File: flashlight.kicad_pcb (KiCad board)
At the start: 2 copper layers, 45 x 120 mm, 23 parts, among them J1 USB_B_Micro, J2 Conn_01x03_Pin, Q2 HSS2333, SW1 SW_DIP_x01, U1 XB4908A, U2 MT3608, U3 TP4057, U4 R6BHC-A05_LED-19-223

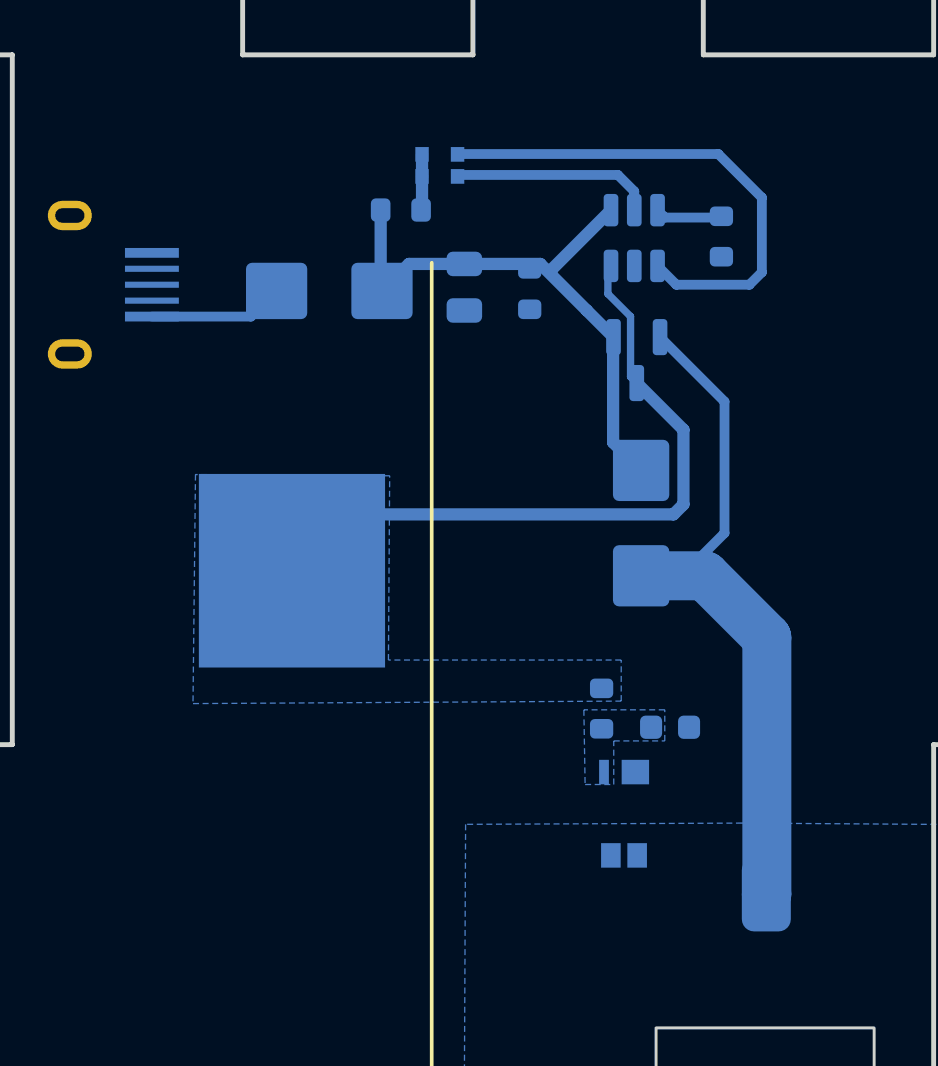
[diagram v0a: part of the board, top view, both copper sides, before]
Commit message: moved TP4057 closer to the VBAT
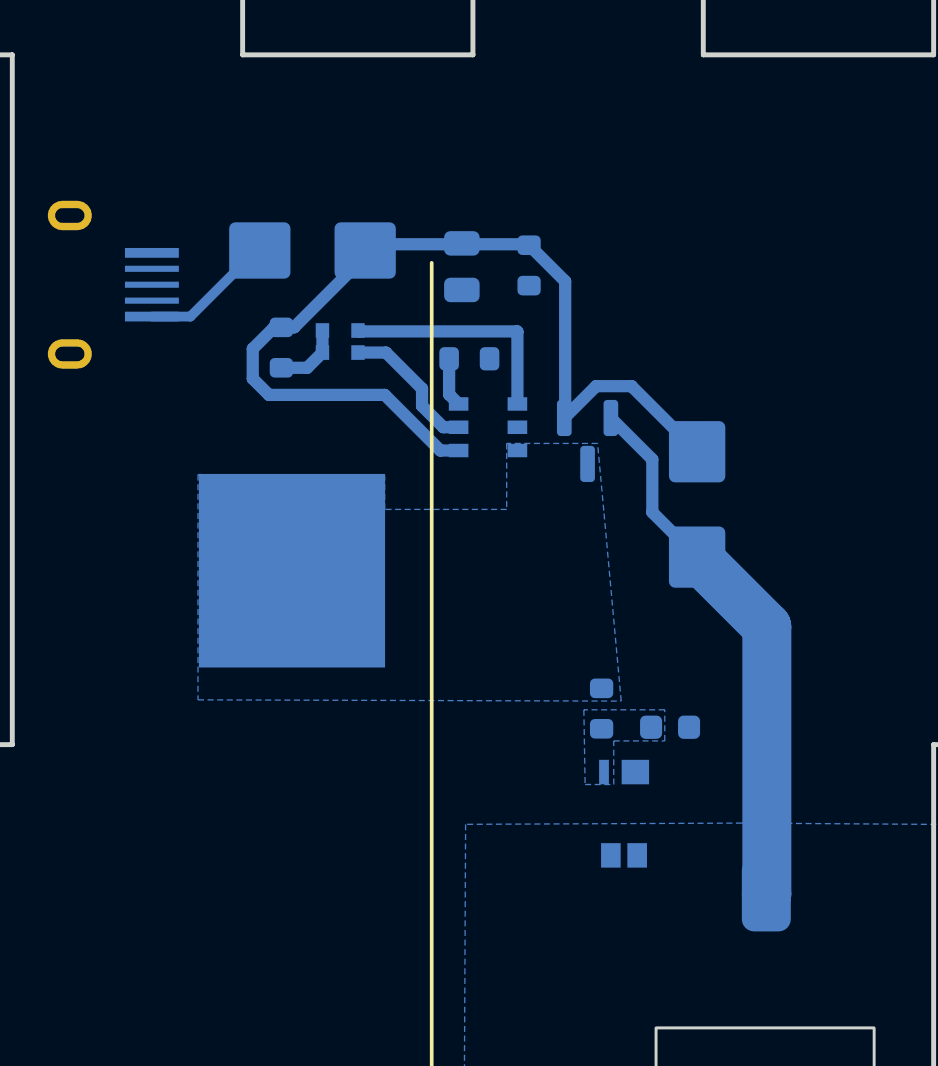
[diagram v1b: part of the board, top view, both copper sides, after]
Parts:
- U3: footprint Package_TO_SOT_SMD:TSOT-23-6 -> SparkFun-Semiconductor-Standard:SOT23-6-Tight
- moved R1 11.4 mm to (97.5, 51.9), turned to 0 degrees
- moved U3 9.76 mm to (98.3, 54.7), turned to 180 degrees
- moved U4 8.26 mm to (93.0, 50.7)
- moved R2 7.44 mm to (89.9, 51.5), turned to -90 degrees
- moved Q2 3.86 mm to (102.4, 55.3)
- moved D4 2.41 mm to (106.8, 57.9)
- moved D1 1.79 mm to (91.1, 47.5)
- moved R4 0.97 mm to (100.0, 48.1)
- moved C1 0.84 mm to (97.2, 48.2)
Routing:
- net Net-(BT1-+): track 28.0 -> 0.00 mm
- net Net-(D1-K): track 23.9 -> 38.8 mm
- net Net-(U3-~{CHRG}): track 21.0 -> 9.48 mm
- net Net-(D4-K): track 29.9 -> 22.1 mm
- net Net-(U3-STDBY): track 8.28 -> 5.78 mm
- net Net-(U3-PROG): track 2.58 -> 2.00 mm
- net Net-(U4-Blue+): track 2.29 -> 2.83 mm
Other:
- board text added: "V2.6"
- board text removed: "V2.5"

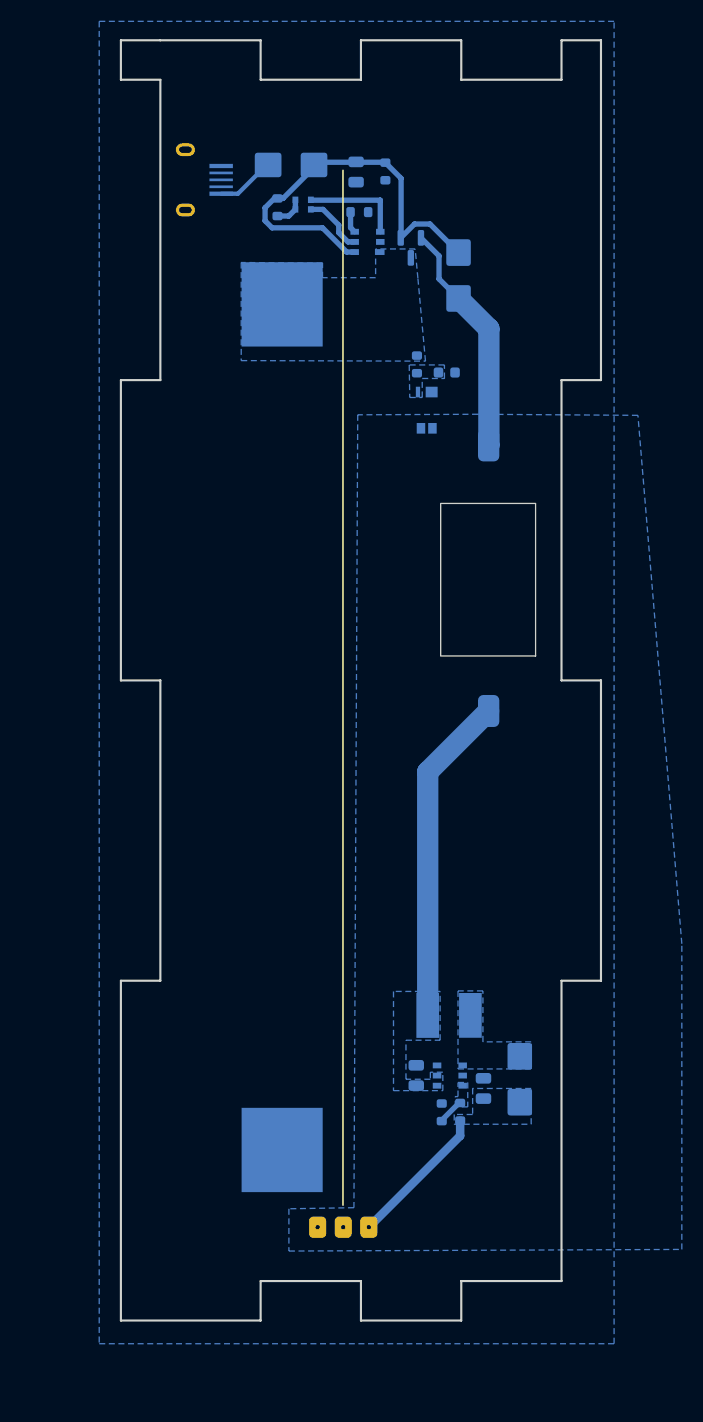
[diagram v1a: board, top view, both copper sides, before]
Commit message: v2.6: board outline 4mm
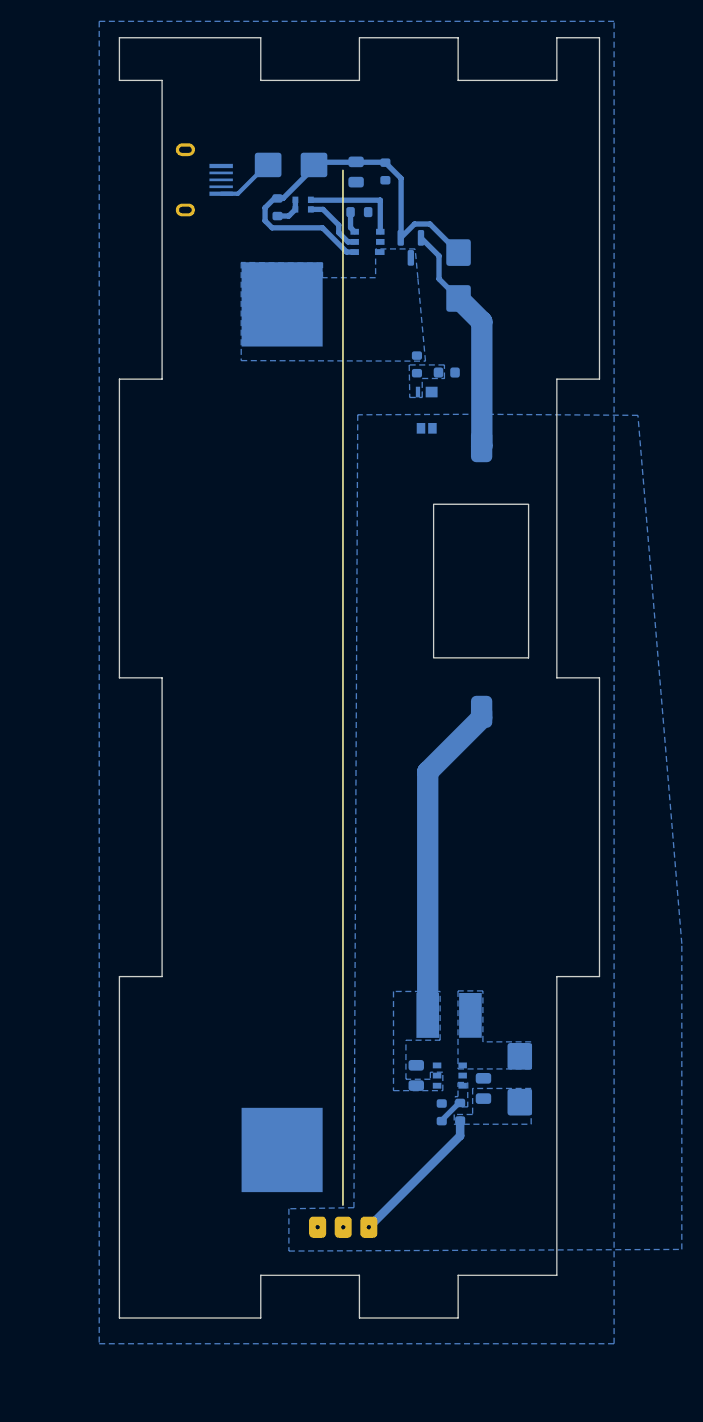
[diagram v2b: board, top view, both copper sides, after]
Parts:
- moved SW1 0.66 mm to (104.5, 79.5)
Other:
- outline, holes or cut-outs redrawn

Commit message: v2.7 boxes
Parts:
- removed SW1: SW_DIP_x01, FlashlightLib:KCD11-2P
- added U5: SS12J01_071, JLCPCB-SS12J01:SW-TH_SHOU-HAN_SS12J01, F.Cu at (109.2, 84.6)
- moved J1 1.30 mm to (82.5, 47.7)
- moved C3 1.20 mm to (102.9, 131.6)
- moved C4 1.20 mm to (109.2, 132.9)
- moved R6 1.20 mm to (105.3, 135.1)
- moved U2 1.20 mm to (106.0, 131.7)
- moved BT1 1.20 mm to (90.3, 99.0)
- moved C1 1.20 mm to (97.2, 47.0)
- moved C2 1.20 mm to (105.7, 65.8)
- moved Q2 1.20 mm to (102.4, 54.1)
- moved R1 1.20 mm to (97.5, 50.7)
- moved R2 1.20 mm to (89.9, 50.3)
- moved R3 1.20 mm to (102.9, 65.0)
- moved U1 1.20 mm to (103.1, 67.6)
- moved U4 1.20 mm to (93.0, 49.5)
- moved D1 1.20 mm to (91.1, 46.3)
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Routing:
- net Net-(U2-EN): track 30.5 -> 49.1 mm
- net Net-(D4-K): track 21.9 -> 36.2 mm
- net VOUT: track 13.5 -> 16.0 mm
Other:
- board size 45 x 120 mm -> 45.2 x 120.2 mm
- board text added: "DO NOT PRINT ON F LAYER!"
- board text added: "V2.7"
- board text added: "ВИМК"
- board text added: "УВІМК"
- board text removed: "V2.6"

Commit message: V3.0 21700 3x8 leds
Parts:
- removed J1: USB_B_Micro, FlashlightLib:USB-1101IPX6-02
- removed J2: Conn_01x03_Pin, FlashlightLib:LED_Strip
- added C4: 22uF/35V, Capacitor_SMD:C_0805_2012Metric, B.Cu at (109.0, 93.3)
- added C5: 10uF/10V, Capacitor_SMD:C_0603_1608Metric, B.Cu at (97.6, 51.8)
- added C6: 10uF/10V, Capacitor_SMD:C_0603_1608Metric, B.Cu at (93.4, 55.1)
- added D10: LED, footprint:LED-SMD_L3.0-W1.4-RD_WHITE, F.Cu at (81.8, 98.9)
- added D11: LED_Pad, footprint:LED-SMD_3P-L5.7-W3.0-RD, F.Cu at (84.4, 94.3)
- added D12: LED_Pad, footprint:LED-SMD_3P-L5.7-W3.0-RD, F.Cu at (95.7, 122.8)
- added D13: LED_Pad, footprint:LED-SMD_3P-L5.7-W3.0-RD, F.Cu at (95.7, 114.9)
- added D14: LED, footprint:LED-SMD_L3.0-W1.4-RD_WHITE, F.Cu at (91.2, 111.1)
- added D15: LED, footprint:LED-SMD_L3.0-W1.4-RD_WHITE, F.Cu at (95.5, 109.4)
- added D16: LED, footprint:LED-SMD_L3.0-W1.4-RD_WHITE, F.Cu at (100.1, 110.9)
- added D17: LED_Pad, footprint:LED-SMD_3P-L5.7-W3.0-RD, F.Cu at (95.7, 104.4)
- added D18: LED, footprint:LED-SMD_L3.0-W1.4-RD_WHITE, F.Cu at (95.9, 99.8)
- added D19: LED, footprint:LED-SMD_L3.0-W1.4-RD_WHITE, F.Cu at (95.6, 97.4)
- added D2: D_Schottky, Diode_SMD:D_SMB, B.Cu at (101.6, 53.9)
- added D20: LED_Pad, footprint:LED-SMD_3P-L5.7-W3.0-RD, F.Cu at (106.4, 94.7)
- added D21: LED, footprint:LED-SMD_L3.0-W1.4-RD_WHITE, F.Cu at (109.3, 99.2)
- added D22: LED_Pad, footprint:LED-SMD_3P-L5.7-W3.0-RD, F.Cu at (106.3, 102.3)
- added D23: LED_Pad, footprint:LED-SMD_3P-L5.7-W3.0-RD, F.Cu at (109.0, 109.3)
- added D24: LED, footprint:LED-SMD_L3.0-W1.4-RD_WHITE, F.Cu at (105.1, 110.8)
- added D25: LED_Pad, footprint:LED-SMD_3P-L5.7-W3.0-RD, F.Cu at (107.5, 114.9)
- added D26: LED, footprint:LED-SMD_L3.0-W1.4-RD_WHITE, F.Cu at (101.0, 114.6)
- added D27: LED_Pad, footprint:LED-SMD_3P-L5.7-W3.0-RD, F.Cu at (100.9, 119.7)
- added D28: LED_Pad, footprint:LED-SMD_3P-L5.7-W3.0-RD, F.Cu at (90.5, 119.7)
- added D3: LED, footprint:LED-SMD_L3.0-W1.4-RD_WHITE, F.Cu at (90.3, 114.6)
- added D6: LED_Pad, footprint:LED-SMD_3P-L5.7-W3.0-RD, F.Cu at (84.0, 115.0)
- added D7: LED, footprint:LED-SMD_L3.0-W1.4-RD_WHITE, F.Cu at (86.5, 111.0)
- added D8: LED_Pad, footprint:LED-SMD_3P-L5.7-W3.0-RD, F.Cu at (82.3, 109.2)
- added D9: LED_Pad, footprint:LED-SMD_3P-L5.7-W3.0-RD, F.Cu at (84.7, 101.8)
- added F2: BSMD1210-150-6V, Fuse:Fuse_1210_3225Metric, B.Cu at (84.9, 44.8)
- added FB1: FerriteBead, Inductor_SMD:L_0805_2012Metric, B.Cu at (87.1, 47.5)
- added G***: LOGO, LOGO, F.Cu at (76.7, 69.3)
- added G***: LOGO, LOGO, F.Cu at (99.0, 74.0)
- added H1: MountingHole, FlashlightLib:M4-insert, F.Cu at (77.7, 59.7)
- added H2: MountingHole, FlashlightLib:M4-insert, F.Cu at (112.5, 45.0)
- added H3: MountingHole, FlashlightLib:M4-insert, F.Cu at (77.7, 155.6)
- added H4: MountingHole, FlashlightLib:M4-insert, F.Cu at (112.5, 155.6)
- added J11: USB_C_Receptacle_USB2.0_16P, footprint:USB-SMD_GT-USB-7070A01, B.Cu at (78.8, 47.5)
- added L2: 10uH, FlashlightLib:L_5.0x5.0, B.Cu at (100.6, 46.6)
- added R20: 5.1k, Resistor_SMD:R_0402_1005Metric, B.Cu at (83.7, 48.7)
- added R21: 5.1k, Resistor_SMD:R_0402_1005Metric, B.Cu at (83.7, 47.3)
- added R5: 33, Resistor_SMD:R_1206_3216Metric_Pad1.30x1.75mm_HandSolder, B.Cu at (106.5, 100.3)
- added R8: 0.05, Resistor_SMD:R_1206_3216Metric, B.Cu at (97.5, 56.3)
- added R9: 33, Resistor_SMD:R_1206_3216Metric_Pad1.30x1.75mm_HandSolder, B.Cu at (106.6, 97.0)
- BT1: footprint FlashlightLib:BH-18650_NoHole -> footprint:BAT-SMD_L82.5.5-W25-BH-21700-B1BJ001
- C1: value 22uF/25V -> 10uF/10V; footprint Capacitor_SMD:C_0805_2012Metric -> Capacitor_SMD:C_0603_1608Metric
- C3: value 22uF/25V -> 22uF/35V
- R1: value 1k -> 33; footprint Resistor_SMD:R_0603_1608Metric -> Resistor_SMD:R_1206_3216Metric_Pad1.30x1.75mm_HandSolder
- R6: value 10k -> 5.23k; footprint Resistor_SMD:R_0603_1608Metric -> Resistor_SMD:R_0805_2012Metric_Pad1.20x1.40mm_HandSolder
- U1: footprint FlashlightLib:XB4908A -> footprint:ESN-4_L2.8-W2.3-LS3.7-BL
- U3: value TP4057 -> TP5000; footprint SparkFun-Semiconductor-Standard:SOT23-6-Tight -> footprint:ESOP-8_L4.9-W3.9-P1.27-LS6.0-BL-EP
- U4: footprint MyFootprints:R6BHC-A05_LED -> footprint:LED-ARRAY-SMD_4P-L1.6-W1.3-BR-FD
- U5: footprint JLCPCB-SS12J01:SW-TH_SHOU-HAN_SS12J01 -> footprint:SW-TH_SHOU-HAN_SS12J01
- moved R1 55.0 mm to (106.5, 105.0)
- moved R7 44.4 mm to (108.0, 90.6)
- moved C4 44.4 mm to (110.1, 88.5)
- moved D5 44.4 mm to (113.5, 87.6)
- moved L1 44.4 mm to (106.8, 81.6)
- moved C3 44.4 mm to (103.8, 87.2)
- moved U2 44.4 mm to (106.9, 87.3)
- moved R6 44.2 mm to (106.0, 90.9)
- moved R4 17.2 mm to (113.2, 58.0)
- moved U5 14.4 mm to (108.3, 70.3)
- moved BT1 8.85 mm to (88.6, 107.7), turned to -90 degrees
- moved U4 6.63 mm to (86.7, 51.6)
- moved Q2 6.10 mm to (101.0, 60.0), turned to 180 degrees
- moved U3 5.88 mm to (92.9, 51.2), turned to -90 degrees
- moved U1 4.69 mm to (107.7, 68.3), turned to 0 degrees
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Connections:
- R1 pad 1: Net-(U3-PROG) -> Net-(D27-A)
- R1 pad 2: GND -> VOUT
- U3 pad 1: Net-(U3-~{CHRG}) -> Net-(D2-K)
- U3 pad 3: Net-(BT1-+) -> Net-(U3-VS)
- U3 pad 4: Net-(D1-K) -> Net-(BT1-+)
- U3 pad 5: Net-(U3-STDBY) -> GND
- U3 pad 6: Net-(U3-PROG) -> Net-(U3-~{STDBY})
- U4 pad 2: Net-(U3-STDBY) -> Net-(U3-~{STDBY})
- U5 pad 1: unconnected-(U5-Pad1) -> Net-(U2-EN)
- U5 pad 3: Net-(U2-EN) -> unconnected-(U5-Pad3)
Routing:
- net Net-(U2-EN): track 49.1 -> 0.00 mm
- net Net-(D28-A): track 0.00 -> 34.9 mm, vias 0 -> 1
- net Net-(D12-A): track 0.00 -> 29.7 mm, vias 0 -> 1
- net Net-(U3-VS): track 0.00 -> 23.0 mm
- net Net-(D27-A): track 0.00 -> 19.4 mm, vias 0 -> 1
- net Net-(D4-K): track 36.2 -> 18.0 mm
- net VOUT: track 16.0 -> 0.00 mm
- net Net-(D2-K): track 0.00 -> 10.5 mm
- net Net-(F2-Pad1): track 0.00 -> 9.40 mm
- net Net-(D16-K): track 0.00 -> 8.06 mm
- net Net-(D24-A): track 0.00 -> 7.22 mm
- net Net-(D6-K): track 0.00 -> 7.21 mm
- net Net-(U3-~{CHRG}): track 9.48 -> 2.83 mm
- net Net-(U3-STDBY): track 5.78 -> 0.00 mm
- net Net-(D20-A): track 0.00 -> 5.39 mm
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- added copper zone on F.Cu, net Earth_Protective
- added copper zone on B.Cu, net Net-(D1-K)
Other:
- board size 45.2 x 120.2 mm -> 46 x 122 mm
- board text added: "+"
- board text added: "V3.0"
- board text removed: "V2.7"

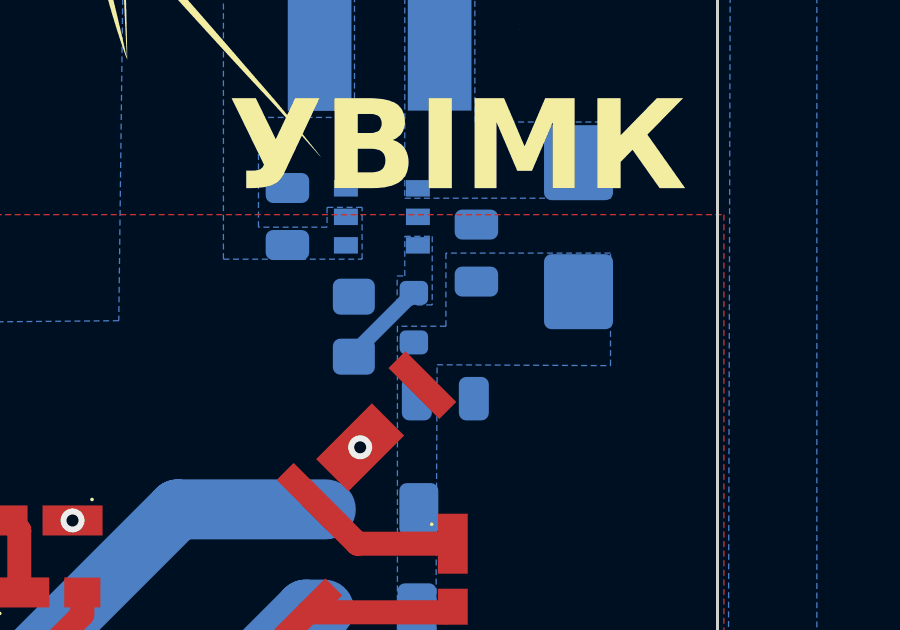
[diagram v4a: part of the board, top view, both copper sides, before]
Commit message: fixed C4 cap issue
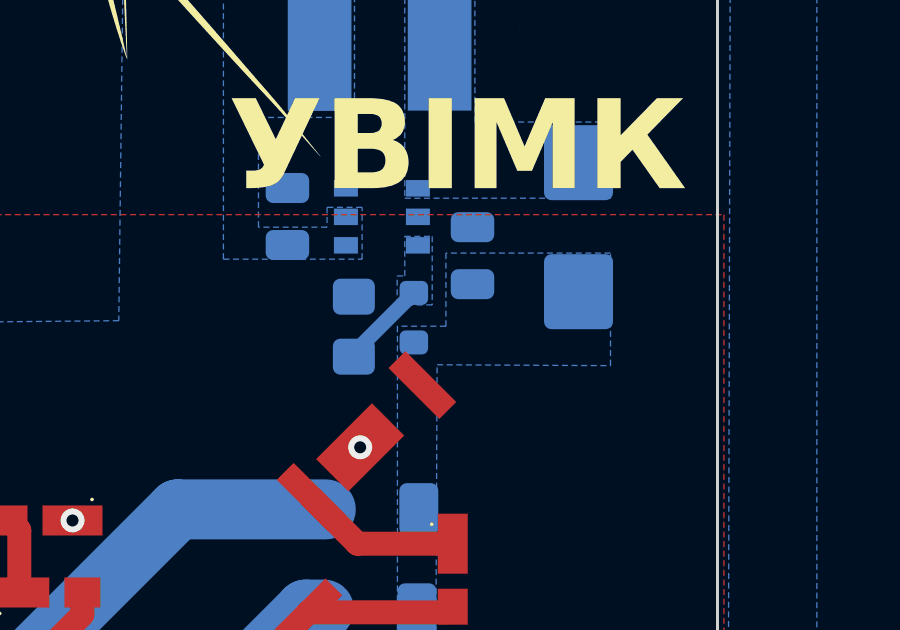
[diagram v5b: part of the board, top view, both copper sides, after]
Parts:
- removed the C4 at (109.0, 93.3)
- removed the C4 at (110.1, 88.5)
- added C4: 22uF/35V, Capacitor_SMD:C_0805_2012Metric, B.Cu at (109.9, 88.5)
